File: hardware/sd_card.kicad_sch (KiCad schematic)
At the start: 2 parts

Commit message: Random changes & LED additions
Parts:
- added D?: GREEN, Diode_SMD:D_0805_2012Metric, symbol Device:LED
- added R?: 10k, Resistor_SMD:R_0603_1608Metric, symbol Device:R_US
- added R?: 1k, Resistor_SMD:R_0603_1608Metric, symbol Device:R_US
- J?: Part Number (none) -> DM3AT-SF-PEJM5; Vendor URL (none) -> https://www.digikey.com/en/products/detail/hirose-electric-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
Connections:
- net GND: now reaches J?.10 (DET_A)
- net ~{DET}: now reaches J?.9 (DET_B)
- net ~{DET}: now also D?.1 (K), R?.2
- new net: D?.2 (A), R?.2
- new net +3.3V: R?.1, R?.1

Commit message: Connector Updates
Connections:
- net +3.3V: now also J?.4 (VDD)
- net GND: now also J?.6 (VSS)
- no-connect marks 0 -> 1
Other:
- moved on the sheet: D?, R?

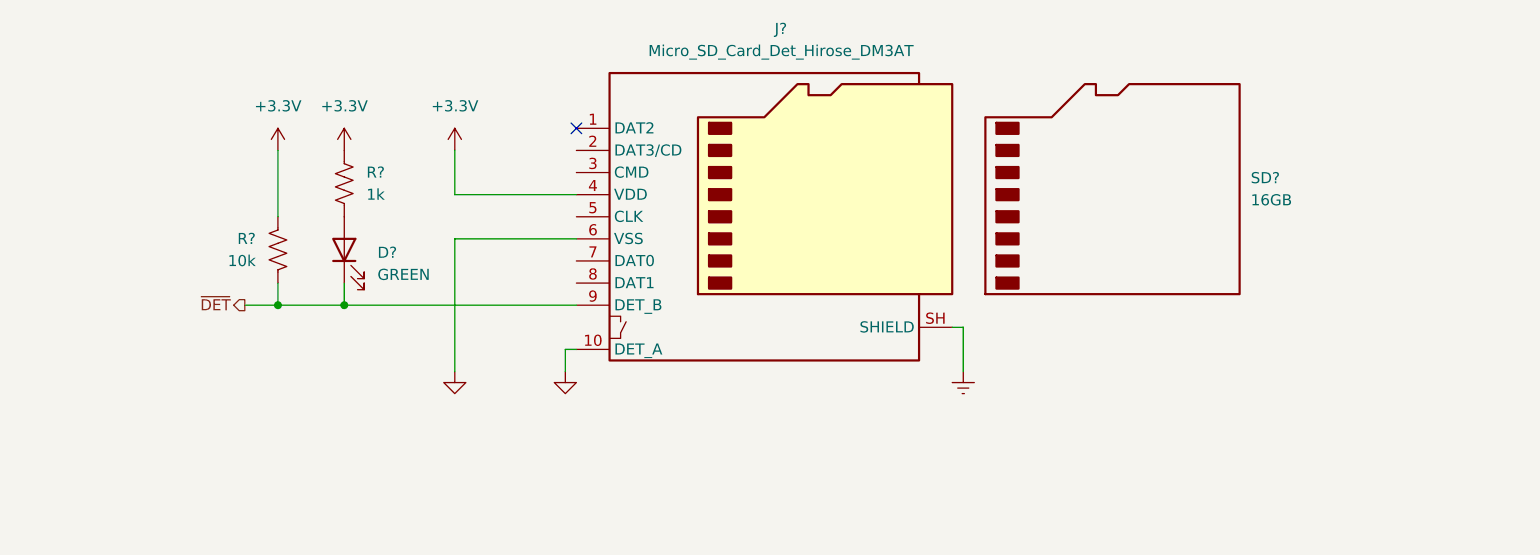
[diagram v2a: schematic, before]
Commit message: SD Card Pull Ups and ESD
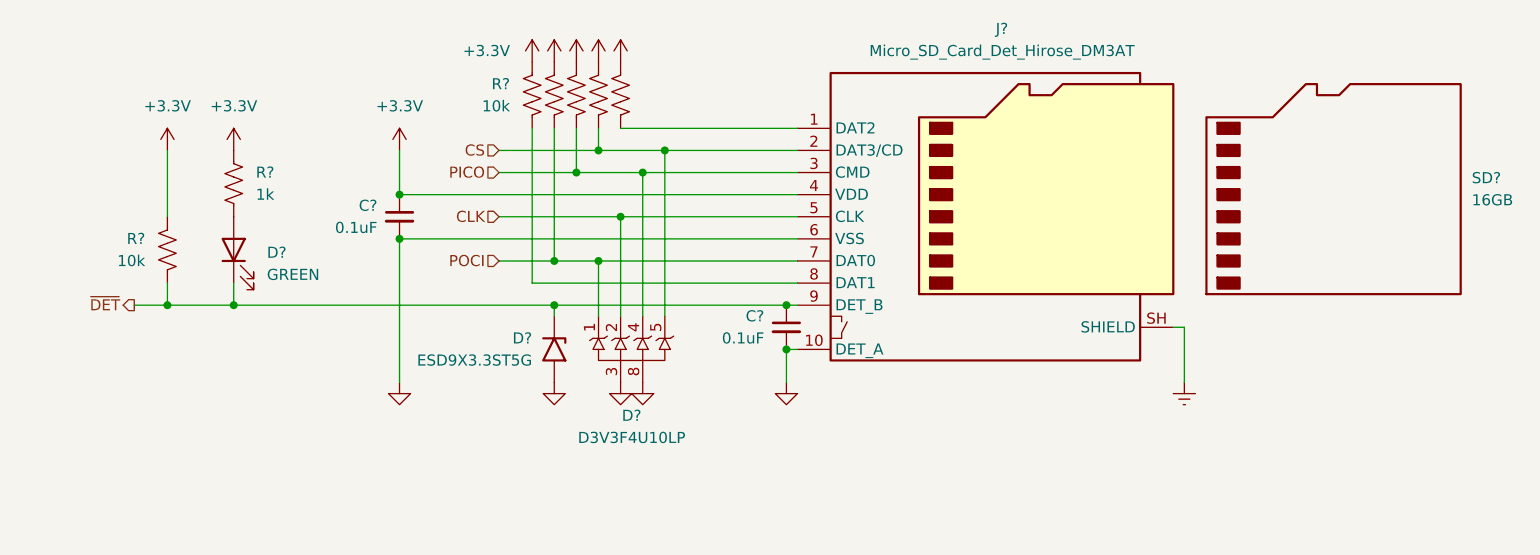
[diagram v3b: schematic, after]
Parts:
- added C? (x2): 0.1uF, Capacitor_SMD:C_0603_1608Metric_Pad1.08x0.95mm_HandSolder, symbol Device:C_Small
- added D?: D3V3F4U10LP, Package_DFN_QFN:Diodes_UDFN-10_1x2.5mm_P0.5mm, symbol Power_Protection:D3V3XA4B10LP
- added D?: ESD9X3.3ST5G, Diode_SMD:D_SOD-923, symbol Diode:SMAJ28A
- added R? (x5): 10k, Resistor_SMD:R_0603_1608Metric, symbol Device:R_US
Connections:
- net +3.3V: now also C?.1, R?.1, R?.1, R?.1, R?.1, R?.1
- net GND: now also C?.2, C?.2, D?.2 (A2), D?.3, D?.8
- net ~{DET}: now also C?.1, D?.1 (A1)
- net at J?.1 (DAT2): now also R?.2
- net CS: now reaches J?.2 (DAT3/CD)
- net CS: now also D?.5, R?.2
- net PICO: now reaches J?.3 (CMD)
- net PICO: now also D?.4, R?.2
- net CLK: now reaches J?.5 (CLK)
- net CLK: now also D?.2
- net POCI: now reaches J?.7 (DAT0)
- net POCI: now also D?.1, R?.2
- net at J?.8 (DAT1): now also R?.2
- new net: D?.10 (NC), D?.6 (NC), D?.7 (NC), D?.9 (NC)
- no-connect marks 1 -> 0
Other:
- moved on the sheet: D?, J?, R?, SD?

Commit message: Fixes and STM32 Pin Assignment Notes
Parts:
- removed C?: 0.1uF, Capacitor_SMD:C_0603_1608Metric_Pad1.08x0.95mm_HandSolder, symbol Device:C_Small
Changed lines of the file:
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@@
 	)
 	(junction
-		(at 144.78 111.76)
-		(diameter 0)
-		(color 0 0 0 0)
-	)
-	(junction
 		(at 118.11 111.76)
 		(diameter 0)
@@
 	)
 	(junction
-		(at 144.78 116.84)
-		(diameter 0)
-		(color 0 0 0 0)
-	)
-	(junction
 		(at 130.81 93.98)
 		(diameter 0)
@@
 	(wire
 		(pts
-			(xy 144.78 111.76) (xy 146.05 111.76)
+			(xy 118.11 111.76) (xy 146.05 111.76)
 		)
 		(stroke
@@
 	(wire
 		(pts
-			(xy 118.11 111.76) (xy 144.78 111.76)
-		)
-		(stroke
-			(width 0)
-			(type default)
-		)
-	)
-	(wire
-		(pts
 			(xy 111.76 96.52) (xy 120.65 96.52)
 		)
@@
 			(hide yes)
 			(show_name no)
-			(do_not_autoplace no)
-			(effects
-				(font
-					(size 1.27 1.27)
-				)
-			)
-		)
-		(pin "1"
-		)
-		(pin "2"
-		)
-		(instances
-			(project "stepping-stone"
-				(path "/793a882e-3f7b-468b-a863-41a1f527e1bf/19dbaeaf-d110-49c5-9d75-50e9003bebb2"
-					(reference "C?")
-					(unit 1)
-				)
-			)
-		)
-	)
-	(symbol
-		(lib_id "Device:C_Small")
-		(at 144.78 114.3 0)
-		(unit 1)
-		(body_style 1)
-		(exclude_from_sim no)
-		(in_bom yes)
-		(on_board yes)
-		(in_pos_files yes)
-		(dnp no)
-		(property "Reference" "C?"
-			(at 142.24 113.03 0)
-			(show_name no)
-			(do_not_autoplace no)
-			(effects
-				(font
-					(size 1.27 1.27)
-				)
-				(justify right)
-			)
-		)
-		(property "Value" "0.1uF"
-			(at 142.24 115.57 0)
-			(show_name no)
-			(do_not_autoplace no)
-			(effects
-				(font
-					(size 1.27 1.27)
-				)
-				(justify right)
-			)
-		)
-		(property "Footprint" "Capacitor_SMD:C_0603_1608Metric_Pad1.08x0.95mm_HandSolder"
-			(at 144.78 114.3 0)
-			(hide yes)
-			(show_name no)
-			(do_not_autoplace no)
-			(effects
-				(font
-					(size 1.27 1.27)
-				)
-			)
-		)
-		(property "Datasheet" ""
-			(at 144.78 114.3 0)
-			(hide yes)
-			(show_name no)
-			(do_not_autoplace no)
-			(effects
-				(font
-					(size 1.27 1.27)
-				)
-			)
-		)
-		(property "Description" "Unpolarized capacitor, small symbol"
-			(at 144.78 114.3 0)
-			(hide yes)
-			(show_name no)
-			(do_not_autoplace no)
-			(effects
-				(font
-					(size 1.27 1.27)
-				)
-			)
-		)
-		(property "Part Number" "CC0603KRX7R9BB104"
-			(at 144.78 114.3 0)
-			(hide yes)
-			(show_name no)
-			(do_not_autoplace no)
-			(effects
-				(font
-					(size 1.27 1.27)
-				)
-			)
-		)
-		(property "Vendor URL" "https://www.digikey.com/en/products/detail/yageo/CC0603KRX7R9BB104/2103082"
-			(at 144.78 114.3 0)
-			(hide yes)
-			(show_name no)
-			(do_not_autoplace no)
-			(effects
-				(font
-					(size 1.27 1.27)
-				)
-			)
-		)
-		(property "Sim.Device" ""
-			(at 144.78 114.3 0)
-			(hide yes)
-			(show_name no)
-			(do_not_autoplace no)
-			(effects
-				(font
-					(size 1.27 1.27)
-				)
-			)
-		)
-		(property "Sim.Pins" ""
-			(at 144.78 114.3 0)
-			(hide yes)
-			(show_name no)

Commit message: Change blue LEDs
Remove extra 5V blue LED driving for simple 3.3V driving instead
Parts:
- added D?: BLUE, Diode_SMD:D_0805_2012Metric, symbol Device:LED
- added R?: 220, Resistor_SMD:R_0603_1608Metric, symbol Device:R_US
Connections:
- net GND: now also D?.1 (K)
- new net: D?.2 (A), R?.2
- new net SD_STATUS: R?.1

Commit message: Add QSPI Flash
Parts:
- gave numbers to parts that had none: 15
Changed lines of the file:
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@@
 		(in_pos_files yes)
 		(dnp no)
-		(property "Reference" "R?"
+		(property "Reference" "R31"
 			(at 71.12 104.1399 0)
 			(show_name no)
@@
 			(project "stepping-stone"
 				(path "/793a882e-3f7b-468b-a863-41a1f527e1bf/19dbaeaf-d110-49c5-9d75-50e9003bebb2"
-					(reference "R?")
+					(reference "R31")
 					(unit 1)
 				)
@@
 		(in_pos_files yes)
 		(dnp no)
-		(property "Reference" "R?"
+		(property "Reference" "R28"
 			(at 120.65 86.3599 0)
 			(hide yes)
@@
 			(project "stepping-stone"
 				(path "/793a882e-3f7b-468b-a863-41a1f527e1bf/19dbaeaf-d110-49c5-9d75-50e9003bebb2"
-					(reference "R?")
+					(reference "R28")
 					(unit 1)
 				)
@@
 		(dnp no)
 		(fields_autoplaced yes)
-		(property "Reference" "R?"
+		(property "Reference" "R30"
 			(at 83.82 96.5199 0)
 			(show_name no)
@@
 			(project "stepping-stone"
 				(path "/793a882e-3f7b-468b-a863-41a1f527e1bf/19dbaeaf-d110-49c5-9d75-50e9003bebb2"
-					(reference "R?")
+					(reference "R30")
 					(unit 1)
 				)
@@
 		(dnp no)
 		(fields_autoplaced yes)
-		(property "Reference" "SD?"
+		(property "Reference" "SD1"
 			(at 223.52 97.1549 0)
 			(show_name no)
@@
 			(project "stepping-stone"
 				(path "/793a882e-3f7b-468b-a863-41a1f527e1bf/19dbaeaf-d110-49c5-9d75-50e9003bebb2"
-					(reference "SD?")
+					(reference "SD1")
 					(unit 1)
 				)
@@
 		(in_pos_files yes)
 		(dnp no)
-		(property "Reference" "R?"
+		(property "Reference" "R25"
 			(at 113.03 86.3599 0)
 			(show_name no)
@@
 			(project "stepping-stone"
 				(path "/793a882e-3f7b-468b-a863-41a1f527e1bf/19dbaeaf-d110-49c5-9d75-50e9003bebb2"
-					(reference "R?")
+					(reference "R25")
 					(unit 1)
 				)
@@
 		(in_pos_files yes)
 		(dnp no)
-		(property "Reference" "D?"
+		(property "Reference" "D13"
 			(at 127 124.46 0)
 			(show_name no)
@@
 			(project "stepping-stone"
 				(path "/793a882e-3f7b-468b-a863-41a1f527e1bf/19dbaeaf-d110-49c5-9d75-50e9003bebb2"
-					(reference "D?")
+					(reference "D13")
 					(unit 1)
 				)
@@
 		(dnp no)
 		(fields_autoplaced yes)
-		(property "Reference" "J?"
+		(property "Reference" "J4"
 			(at 169.545 80.01 0)
 			(show_name no)
@@
 			(project "stepping-stone"
 				(path "/793a882e-3f7b-468b-a863-41a1f527e1bf/19dbaeaf-d110-49c5-9d75-50e9003bebb2"
-					(reference "J?")
+					(reference "J4")
 					(unit 1)
 				)
@@
 		(in_pos_files yes)
 		(dnp no)
-		(property "Reference" "R?"
+		(property "Reference" "R29"
 			(at 123.19 86.3599 0)
 			(hide yes)
@@
 			(project "stepping-stone"
 				(path "/793a882e-3f7b-468b-a863-41a1f527e1bf/19dbaeaf-d110-49c5-9d75-50e9003bebb2"
-					(reference "R?")
+					(reference "R29")
 					(unit 1)
 				)
@@
 		(in_pos_files yes)
 		(dnp no)
-		(property "Reference" "D?"
+		(property "Reference" "D14"
 			(at 115.57 115.57 90)
 			(show_name no)
@@
 			(project "stepping-stone"
 				(path "/793a882e-3f7b-468b-a863-41a1f527e1bf/19dbaeaf-d110-49c5-9d75-50e9003bebb2"
-					(reference "D?")
+					(reference "D14")
 					(unit 1)
 				)
@@
 		(in_pos_files yes)
 		(dnp no)
-		(property "Reference" "R?"
+		(property "Reference" "R26"
 			(at 115.57 86.3599 0)
 			(hide yes)
@@
 			(project "stepping-stone"
 				(path "/793a882e-3f7b-468b-a863-41a1f527e1bf/19dbaeaf-d110-49c5-9d75-50e9003bebb2"
-					(reference "R?")
+					(reference "R26")
 					(unit 1)
 				)
@@
 		(in_pos_files yes)
 		(dnp no)
-		(property "Reference" "D?"
+		(property "Reference" "D15"
 			(at 77.47 132.3974 90)
 			(show_name no)
@@
 			(project "stepping-stone"
 				(path "/793a882e-3f7b-468b-a863-41a1f527e1bf/19dbaeaf-d110-49c5-9d75-50e9003bebb2"
-					(reference "D?")
+					(reference "D15")
 					(unit 1)
 				)
@@
 		(in_pos_files yes)
 		(dnp no)
-		(property "Reference" "R?"
+		(property "Reference" "R27"
 			(at 118.11 86.3599 0)
 			(hide yes)
@@
 			(project "stepping-stone"
 				(path "/793a882e-3f7b-468b-a863-41a1f527e1bf/19dbaeaf-d110-49c5-9d75-50e9003bebb2"
-					(reference "R?")
+					(reference "R27")
 					(unit 1)
 				)
@@
 		(in_pos_files yes)
 		(dnp no)
-		(property "Reference" "R?"
+		(property "Reference" "R32"
 			(at 78.74 120.6499 0)
 			(show_name no)
@@
 			(project "stepping-stone"
 				(path "/793a882e-3f7b-468b-a863-41a1f527e1bf/19dbaeaf-d110-49c5-9d75-50e9003bebb2"
-					(reference "R?")
+					(reference "R32")
 					(unit 1)
 				)
@@
 		(dnp no)
 		(fields_autoplaced yes)
-		(property "Reference" "D?"
+		(property "Reference" "D12"
 			(at 85.09 105.7274 90)
 			(show_name no)
@@
 			(project "stepping-stone"
 				(path "/793a882e-3f7b-468b-a863-41a1f527e1bf/19dbaeaf-d110-49c5-9d75-50e9003bebb2"
-					(reference "D?")
+					(reference "D12")
 					(unit 1)
 				)
@@
 		(in_pos_files yes)
 		(dnp no)
-		(property "Reference" "C?"
+		(property "Reference" "C17"
 			(at 97.79 100.33 0)
 			(show_name no)
@@
 			(project "stepping-stone"
 				(path "/793a882e-3f7b-468b-a863-41a1f527e1bf/19dbaeaf-d110-49c5-9d75-50e9003bebb2"
-					(reference "C?")
+					(reference "C17")
 					(unit 1)
 				)

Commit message: Limit Switches and CAN Bus
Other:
- company: (none) -> Jacob Wigent
- title: (none) -> SD Card
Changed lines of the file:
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@@
 	(generator "eeschema")
 	(generator_version "10.0")
-	(paper "A4")
+	(paper "A")
+	(title_block
+		(title "SD Card")
+		(rev "A")
+		(company "Jacob Wigent")
+	)
 	(junction
 		(at 128.27 96.52)

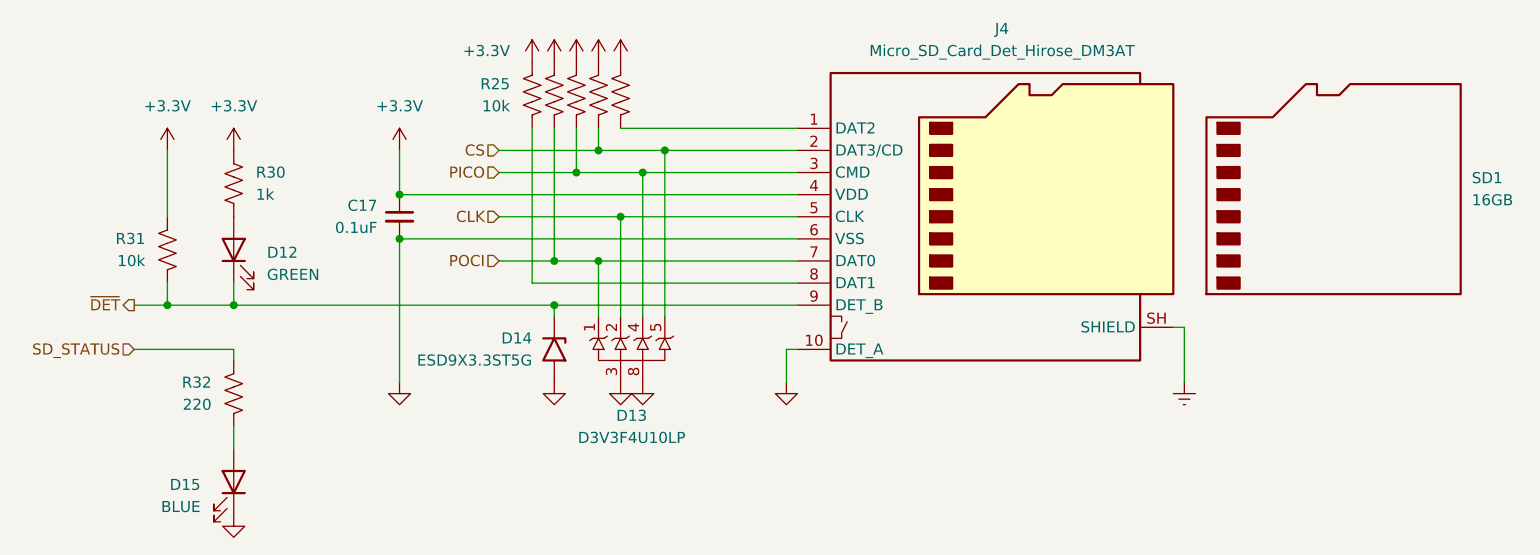
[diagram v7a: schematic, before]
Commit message: Update logic level TVS diode part
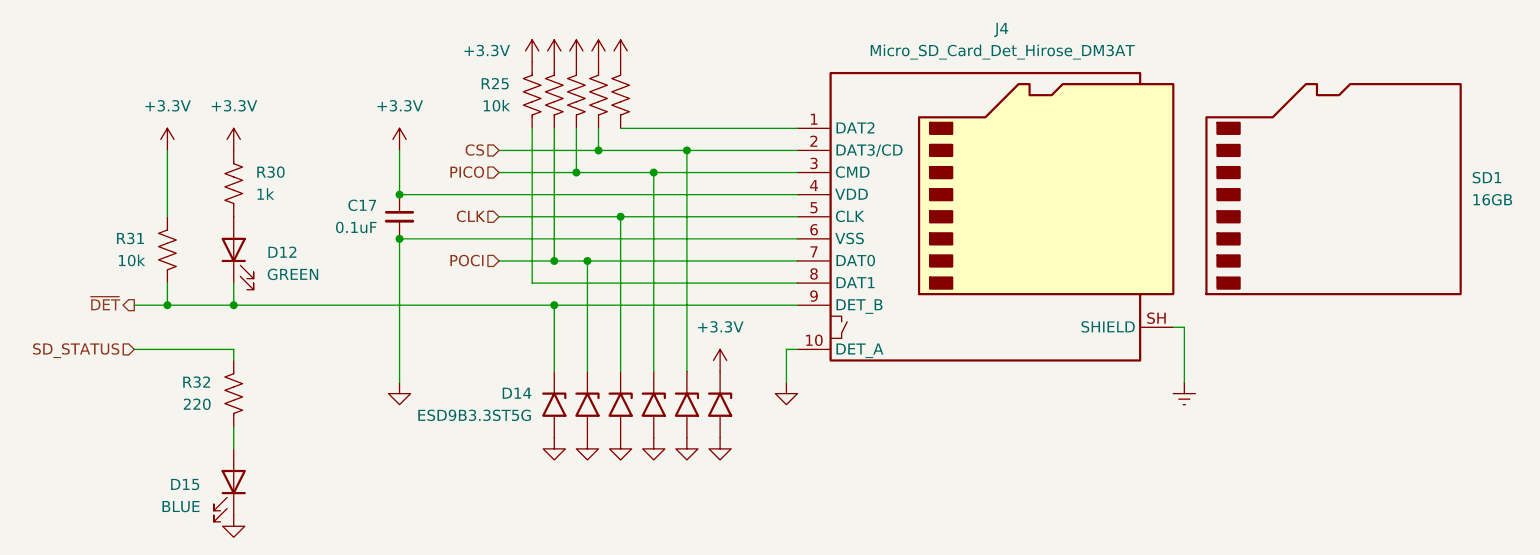
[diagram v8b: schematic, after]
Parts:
- removed D13: D3V3F4U10LP, Package_DFN_QFN:Diodes_UDFN-10_1x2.5mm_P0.5mm, symbol Power_Protection:D3V3XA4B10LP
- added D? (x5): ESD9B3.3ST5G, Diode_SMD:D_SOD-923, symbol Diode:SMAJ28A
- D14: value ESD9X3.3ST5G -> ESD9B3.3ST5G; Part Number ESD9X3.3ST5G -> ESD9B3.3ST5G; Vendor URL https://www.digikey.com/en/products/detail/onsemi/ESD9X3-3S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 -> https://www.digikey.com/en/products/detail/onsemi/ESD9B3-3S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
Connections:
- net +3.3V: now also D?.1 (A1)
- net CLK: now also D?.1 (A1)
- net CS: now also D?.1 (A1)
- net GND: now also D?.2 (A2), D?.2 (A2), D?.2 (A2), D?.2 (A2), D?.2 (A2)
- net PICO: now also D?.1 (A1)
- net POCI: now also D?.1 (A1)
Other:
- moved on the sheet: D14
